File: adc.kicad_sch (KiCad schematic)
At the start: 86 parts, among them J501 Screw_Terminal_01x02, J502 Screw_Terminal_01x02, J503 Screw_Terminal_01x02, J504 Screw_Terminal_01x02, J505 Screw_Terminal_01x02, J506 Screw_Terminal_01x02, U501 ADS131M08IRSNR, U502 TSV914AIDR, U503 TSV914AIDR, U504 TSV914AIDR

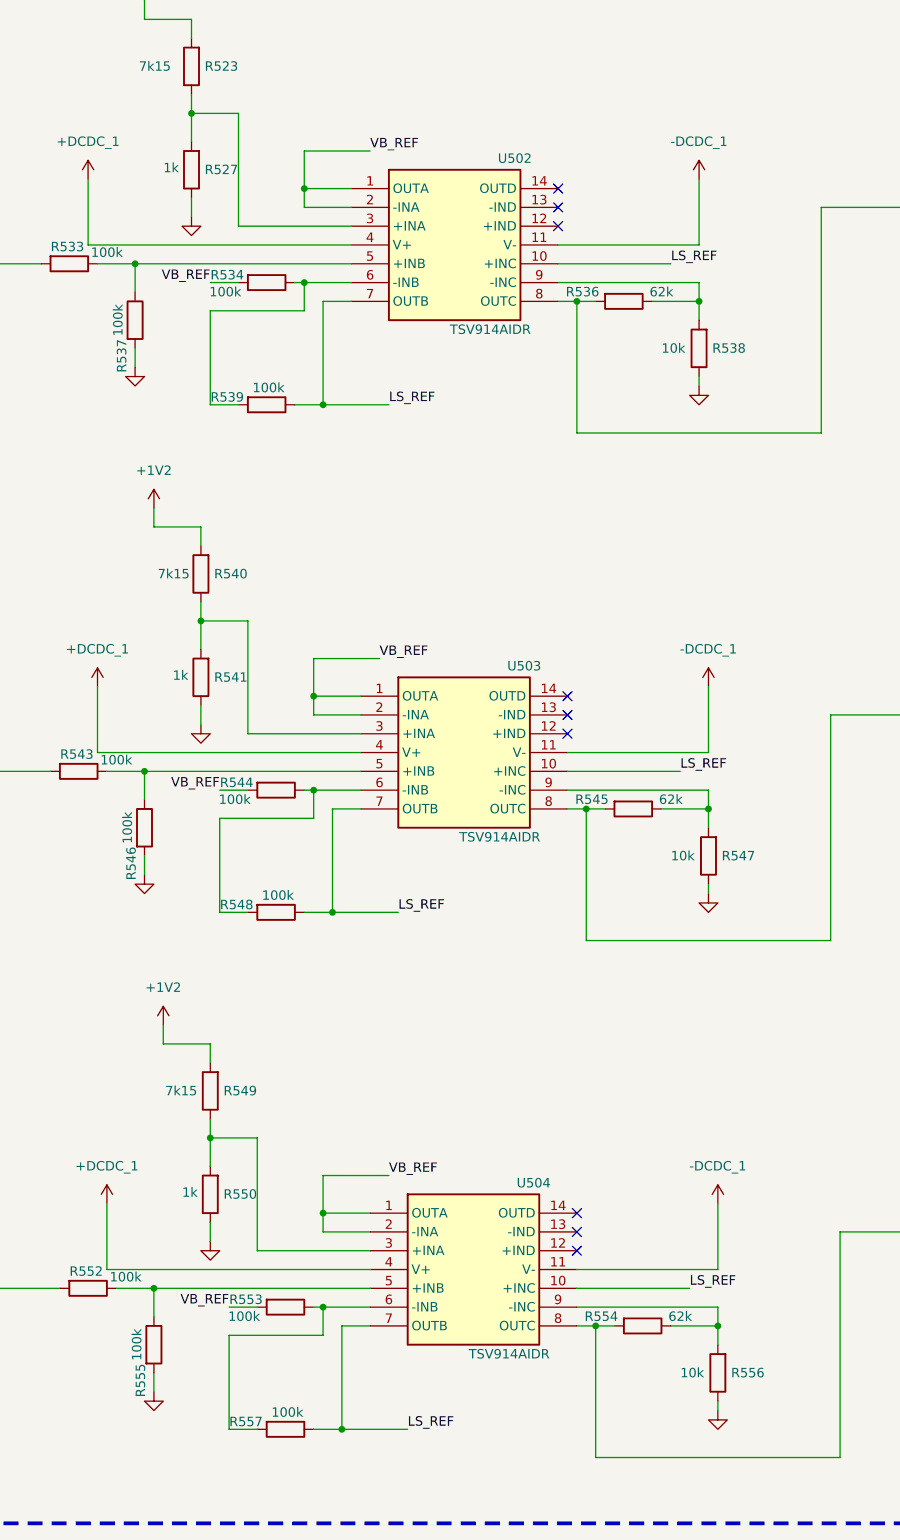
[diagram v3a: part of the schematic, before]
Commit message: routing of CTs complete
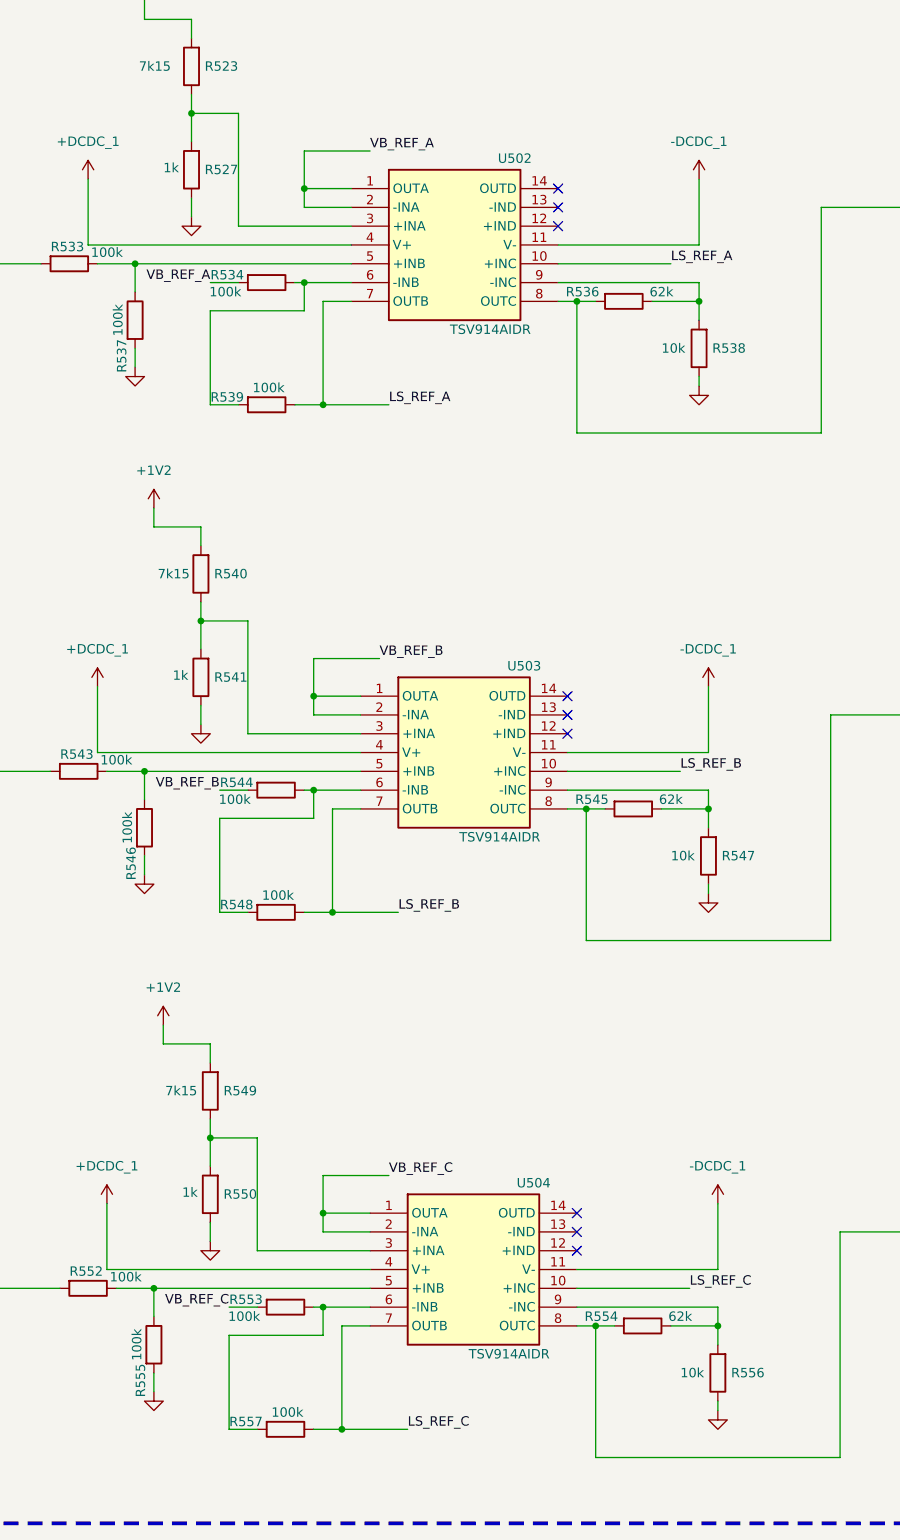
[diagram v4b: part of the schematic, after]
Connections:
- removed net LS_REF: R539.1, R548.1, R557.1, U502.10 (+INC), U502.7 (OUTB), U503.10 (+INC), U503.7 (OUTB), U504.10 (+INC), U504.7 (OUTB)
- removed net VB_REF: R534.2, R544.2, R553.2, U502.1 (OUTA), U502.2 (-INA), U503.1 (OUTA), U503.2 (-INA), U504.1 (OUTA), U504.2 (-INA)
- new net LS_REF_A: R539.1, U502.10 (+INC), U502.7 (OUTB)
- new net LS_REF_B: R548.1, U503.10 (+INC), U503.7 (OUTB)
- new net LS_REF_C: R557.1, U504.10 (+INC), U504.7 (OUTB)
- new net VB_REF_A: R534.2, U502.1 (OUTA), U502.2 (-INA)
- new net VB_REF_B: R544.2, U503.1 (OUTA), U503.2 (-INA)
- new net VB_REF_C: R553.2, U504.1 (OUTA), U504.2 (-INA)
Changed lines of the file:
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@@
 		)
 	)
-	(label "LS_REF"
+	(label "LS_REF_C"
 		(at 139.7 347.98 0)
 		(fields_autoplaced yes)
@@
 		)
 	)
-	(label "VB_REF"
+	(label "VB_REF_A"
 		(at 74.93 212.09 180)
 		(fields_autoplaced yes)
@@
 		)
 	)
-	(label "VB_REF"
+	(label "VB_REF_A"
 		(at 96.52 194.31 0)
 		(fields_autoplaced yes)
@@
 		)
 	)
-	(label "LS_REF"
+	(label "LS_REF_A"
 		(at 137.16 209.55 0)
 		(fields_autoplaced yes)
@@
 		)
 	)
-	(label "LS_REF"
+	(label "LS_REF_A"
 		(at 99.06 228.6 0)
 		(fields_autoplaced yes)
@@
 		)
 	)
-	(label "LS_REF"
+	(label "LS_REF_B"
 		(at 138.43 278.13 0)
 		(fields_autoplaced yes)
@@
 		)
 	)
-	(label "VB_REF"
+	(label "VB_REF_B"
 		(at 97.79 262.89 0)
 		(fields_autoplaced yes)
@@
 		)
 	)
-	(label "VB_REF"
+	(label "VB_REF_C"
 		(at 99.06 332.74 0)
 		(fields_autoplaced yes)
@@
 		)
 	)
-	(label "LS_REF"
+	(label "LS_REF_B"
 		(at 100.33 297.18 0)
 		(fields_autoplaced yes)
@@
 		)
 	)
-	(label "VB_REF"
+	(label "VB_REF_B"
 		(at 76.2 280.67 180)
 		(fields_autoplaced yes)
@@
 		)
 	)
-	(label "LS_REF"
+	(label "LS_REF_C"
 		(at 101.6 367.03 0)
 		(fields_autoplaced yes)
@@
 		)
 	)
-	(label "VB_REF"
+	(label "VB_REF_C"
 		(at 77.47 350.52 180)
 		(fields_autoplaced yes)

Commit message: erc with no error
1. Updated footprint for ADS
2. fixed constraints
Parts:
- U501: footprint EMS:ADS131M08IPBS-WQFN-A -> EMS:ADS131M08IRSNR-QFN40
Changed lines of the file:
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@@
 			)
 		)
-		(property "Footprint" "EMS:ADS131M08IPBS-WQFN-A"
+		(property "Footprint" "EMS:ADS131M08IRSNR-QFN40"
 			(at 378.46 249.682 0)
 			(effects

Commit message: update to OpAmp setup and bug fix
1. Fixed incorrect opamp connection
2. Improved RF connectivity for BLE
3. Fixed minor bugs
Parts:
- removed R523, R540, R549: 7k15, Resistor_SMD:R_0603_1608Metric, symbol Device:R
- removed R527, R541, R550: 1k, Resistor_SMD:R_0603_1608Metric, symbol Device:R
- removed R534, R537, R543, R544, R546, R548, R552, R553, R555, R557: 100k, Resistor_SMD:R_0603_1608Metric, symbol Device:R
- removed R545, R554: 62k, Resistor_SMD:R_0603_1608Metric, symbol Device:R
- removed R547, R556: 10k, Resistor_SMD:R_0603_1608Metric, symbol Device:R
- removed U502, U503, U504: TSV914AIDR, EMS:TSV914AIDR-SOIC-14, symbol EMS:TSV914AIDR
- added R532, R535: 15k, Resistor_SMD:R_0603_1608Metric, symbol Device:R
- added U502, U503, U504: TSV911ILT, EMS:TSV911ILT_SOT23-5, symbol EMS:TSV911ILT
- R533, R539: value 100k -> 10k; Distributor_Link https://www.mouser.com/ProductDetail/Vishay-Dale/CRCW0603100KFKEE?qs=%252B6g0mu59x7I1D%252BO0qMg%252Bjg%3D%3D -> https://www.mouser.com/ProductDetail/Vishay-Dale/CRCW060310K0FKEI?qs=3qWEzBg5KnKofE%252B8acPBRA%3D%3D; Manufacturer_Part_Number CRCW0603100KFKEE -> CRCW060310K0FKEI
- R536: value 62k -> 10k; Distributor_Link https://www.mouser.com/ProductDetail/Panasonic/ERJ-H3EF6202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 -> https://www.mouser.com/ProductDetail/Vishay-Dale/CRCW060310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; Manufacturer_Name Panasonic -> Vishay/Dale; Manufacturer_Part_Number ERJ-H3EF6202V -> CRCW060310K0FKEI
- R538: value 10k -> 15k; Distributor_Link https://www.mouser.com/ProductDetail/Vishay-Dale/CRCW060310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 -> https://www.mouser.com/ProductDetail/Panasonic/ERJ-S03F1502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; Manufacturer_Name Vishay/Dale -> Panasonic; Manufacturer_Part_Number CRCW060310K0FKEI -> ERJ-S03F1502V
- renumbered R524 to R523, R525 to R524, R526 to R525, R528 to R526, R529 to R527, R530 to R528, R531 to R529, R532 to R530, R535 to R531, R542 to R534, R551 to R537
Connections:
- net +DCDC_1: now also U502.5 (VCC+), U503.5 (VCC+), U504.5 (VCC+)
- net -DCDC_1: now also U502.2 (VCC-), U503.2 (VCC-), U504.2 (VCC-)
- net GND: now also R533.2, R536.2, R539.2; no longer R538.1
- net CT_PhaseA_IN: now reaches J504.1 (Pin_1)
- net CT_PhaseA_IN: now also U502.3 (IN+); no longer R533.2
- net CT_PhaseC_Amp_OUT: now reaches R537.2
- net CT_PhaseC_Amp_OUT: now also R538.2, U504.1 (OUT)
- net CT_PhaseC_IN: now reaches J506.1 (Pin_1)
- net CT_PhaseC_IN: now also U504.3 (IN+)
- net at R536.1: now also R535.1, U503.4 (IN-); no longer R538.2
- net CT_PhaseB_Amp_OUT: now reaches R534.2
- net CT_PhaseB_Amp_OUT: now also R535.2, U503.1 (OUT)
- net CT_PhaseA_Amp_OUT: now reaches R528.2
- net CT_PhaseA_Amp_OUT: now also R532.2, U502.1 (OUT); no longer R536.2
- net CT_PhaseB_IN: now reaches J505.1 (Pin_1)
- net CT_PhaseB_IN: now also U503.3 (IN+)
- net at R533.1: now also R532.1, U502.4 (IN-)
- net LS_REF_A: no longer names the net of R539.1
- net LS_REF_A: now also R538.1, U504.4 (IN-)
- no-connect marks 15 -> 6

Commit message: finalized design v1.0.0
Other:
- note added: "[3] ADC"
- title: (none) -> Energy Monitoring System
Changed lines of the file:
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@@
 	(paper "A2")
 	(title_block
+		(title "Energy Monitoring System")
 		(rev "v1.0.0")
 		(company "Manufacturing Innovation Network Laboratory (MINLab)")
+		(comment 1 "Developed by Vignesh Selvaraj")
 	)
 	(junction
@@
 		)
 	)
+	(text "[3] ADC\n"
+		(exclude_from_sim no)
+		(at 528.32 32.258 0)
+		(effects
+			(font
+				(size 11.43 11.43)
+				(thickness 2.286)
+				(bold yes)
+			)
+		)
+	)
 	(text "Voltage Input"
 		(exclude_from_sim no)
@@
 			)
 		)
-		(property "Datasheet" "https://www.phoenixcontact.com/us/products/1548128/pdf"
+		(property "Datasheet" "https://www.mouser.com/manufacturer/phoenix-contact/"
 			(at 29.21 209.55 0)
 			(effects
@@
 			)
 		)
-		(property "Datasheet" "https://www.phoenixcontact.com/us/products/1548128/pdf"
+		(property "Datasheet" "https://www.mouser.com/manufacturer/phoenix-contact/"
 			(at 29.21 128.27 0)
 			(effects
@@
 			)
 		)
-		(property "Datasheet" "https://www.phoenixcontact.com/us/products/1548128/pdf"
+		(property "Datasheet" "https://www.mouser.com/manufacturer/phoenix-contact/"
 			(at 31.75 347.98 0)
 			(effects
@@
 			)
 		)
-		(property "Datasheet" "https://www.phoenixcontact.com/us/products/1548128/pdf"
+		(property "Datasheet" "https://www.mouser.com/manufacturer/phoenix-contact/"
 			(at 30.48 278.13 0)
 			(effects
@@
 			)
 		)
-		(property "Datasheet" "https://www.phoenixcontact.com/us/products/1548128/pdf"
+		(property "Datasheet" "https://www.mouser.com/manufacturer/phoenix-contact/"
 			(at 29.21 52.07 0)
 			(effects
@@
 			)
 		)
-		(property "Datasheet" "https://www.phoenixcontact.com/us/products/1548128/pdf"
+		(property "Datasheet" "https://www.mouser.com/manufacturer/phoenix-contact/"
 			(at 29.21 90.17 0)
 			(effects

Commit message: v2.0 schematics updated
1. Need to be tested for errors
2. PCB layout is not started yet
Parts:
- renumbered C501 to C601, C502 to C602, C503 to C603, C504 to C604, C505 to C605, C506 to C606, C507 to C607, C508 to C608, C509 to C609, C510 to C610, C511 to C611, C512 to C612, C513 to C613, C514 to C614, C515 to C615, C516 to C616, C517 to C617, C518 to C618, C519 to C619, J501 to J601, J502 to J602, J503 to J603, J504 to J604, J505 to J605, J506 to J606, R501 to R601, R502 to R602, R503 to R603, R504 to R604, R505 to R605, R506 to R606, R507 to R607, R508 to R608, R509 to R609, R510 to R610, R511 to R611, R512 to R612, R513 to R613, R514 to R614, R515 to R615, R516 to R616, R517 to R617, R518 to R618, R519 to R619, R520 to R620, R521 to R621, R522 to R622, R523 to R623, R524 to R624, R525 to R625, R526 to R626, R527 to R627, R528 to R628, R529 to R629, R530 to R630, R531 to R631, R532 to R632, R533 to R633, R534 to R634, R535 to R635, R536 to R636, R537 to R637, R538 to R638, R539 to R639, U501 to U601, U502 to U602, U503 to U603, U504 to U604
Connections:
- net ADS_SPI1_SCK renamed ADS_SPI_SCK
